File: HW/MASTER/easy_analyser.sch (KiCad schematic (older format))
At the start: 39 parts, among them J2 Header_02x10_Male, U1 IP425x-8, U2 IP425x-8, U3 CY7C68013A, U4 MIC5317, U5 24LC01, Y1 24MHz

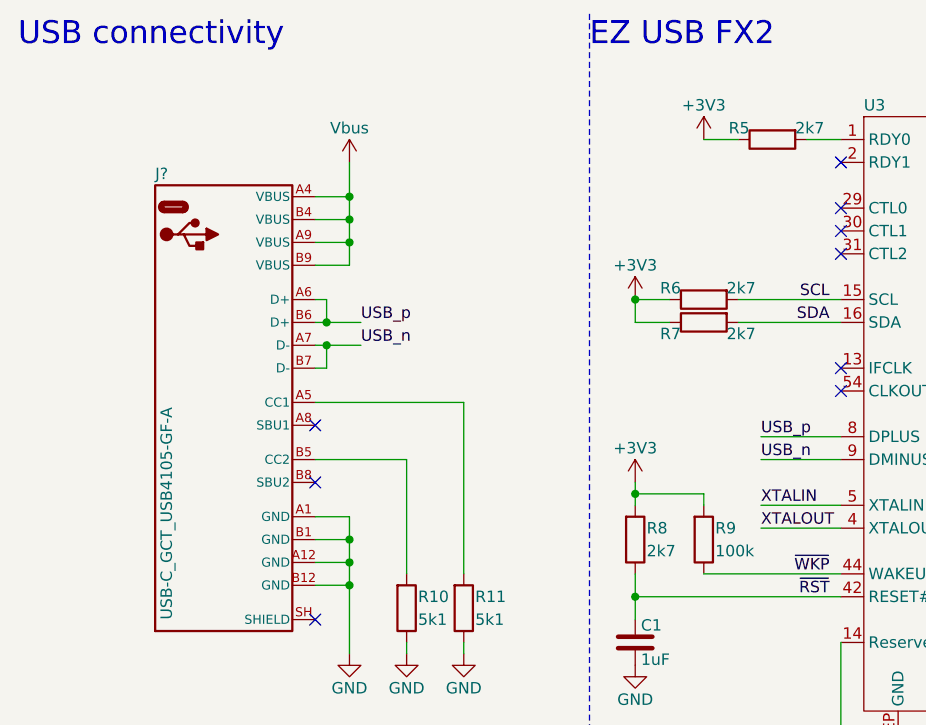
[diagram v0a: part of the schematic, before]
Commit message: Associated symbols with footprints
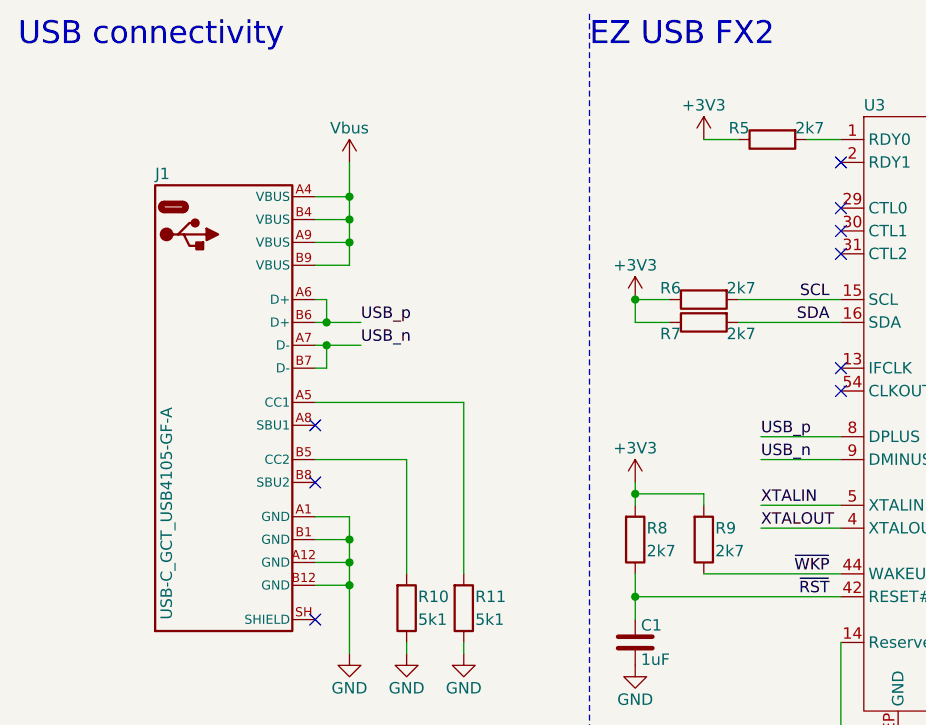
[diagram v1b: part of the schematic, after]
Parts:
- C1, C10, C11, C12, C13, C14, C15, C16, C2, C3, C4, C5, C6, C7, C8, C9: footprint (none) -> capacitors:C_0603
- J1: renamed from J?; footprint USB-C_JAE_USB4105-GF-A -> connectors_USB:GCT_USB4105
- J2: footprint (none) -> connectors_box_headers:WURTH_61202021721
- LD1, LD2: footprint (none) -> leds:LD_0603
- R1, R2, R3, R4: footprint (none) -> resistors:BOURNS_CAY16-J4_1206-4
- R10, R11, R12, R13, R5, R6, R7, R8: footprint (none) -> resistors:R_0603
- R9: value 100k -> 2k7; footprint (none) -> resistors:R_0603
- U1, U2: footprint (none) -> packages_DFN:DFN3.30X1.35X0.55-16
- U3: footprint (none) -> packages_QFN:QFN0.5P8.00X8.00X0.90-56
- U4: footprint (none) -> packages_SOT:SOT230.9P2.7X2.9-5
- U5: footprint (none) -> packages_MSOP:MSOP0.65P6.40X1.20-8
- Y1: footprint (none) -> crystals-oscillators:XTAL3.20X2.50X0.80

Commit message: Finished PCB design
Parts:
- added J3: header_01x02_male, connectors_header:HDRVTH2P2.54_1x02, symbol headers:header_01x02_male
- J2: value Header_02x10_Male -> header_02x10_male
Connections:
- net SCL: now also J3.2
- net SDA: now also J3.1
- net USB_n renamed USB_N
- net USB_p renamed USB_P
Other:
- moved on the sheet: C10, C11, C12, U4, U5

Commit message: Fixed library reference
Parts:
- J2: symbol headers:Header_02x10_Male -> headers:header_02x10_male
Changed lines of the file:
@@
 100nF for each\nVDD pin + 1uF\nfor each VDDA\npin.
 $Comp
-L headers:Header_02x10_Male J2
+L headers:header_02x10_male J2
 U 1 1 640C1D2E
 P 10500 3450
